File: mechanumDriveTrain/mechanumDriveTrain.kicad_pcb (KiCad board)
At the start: 4 copper layers, 88.9 x 99 mm, 38 parts, among them IC1 TCAN3414DR, J1 XT30U-M, J2 BM02B-SRSS-TB, J3 5 pin dupont, J4 5 pin dupont, U1 Teensy 4.1, U2 LD1117S50TR_SOT223

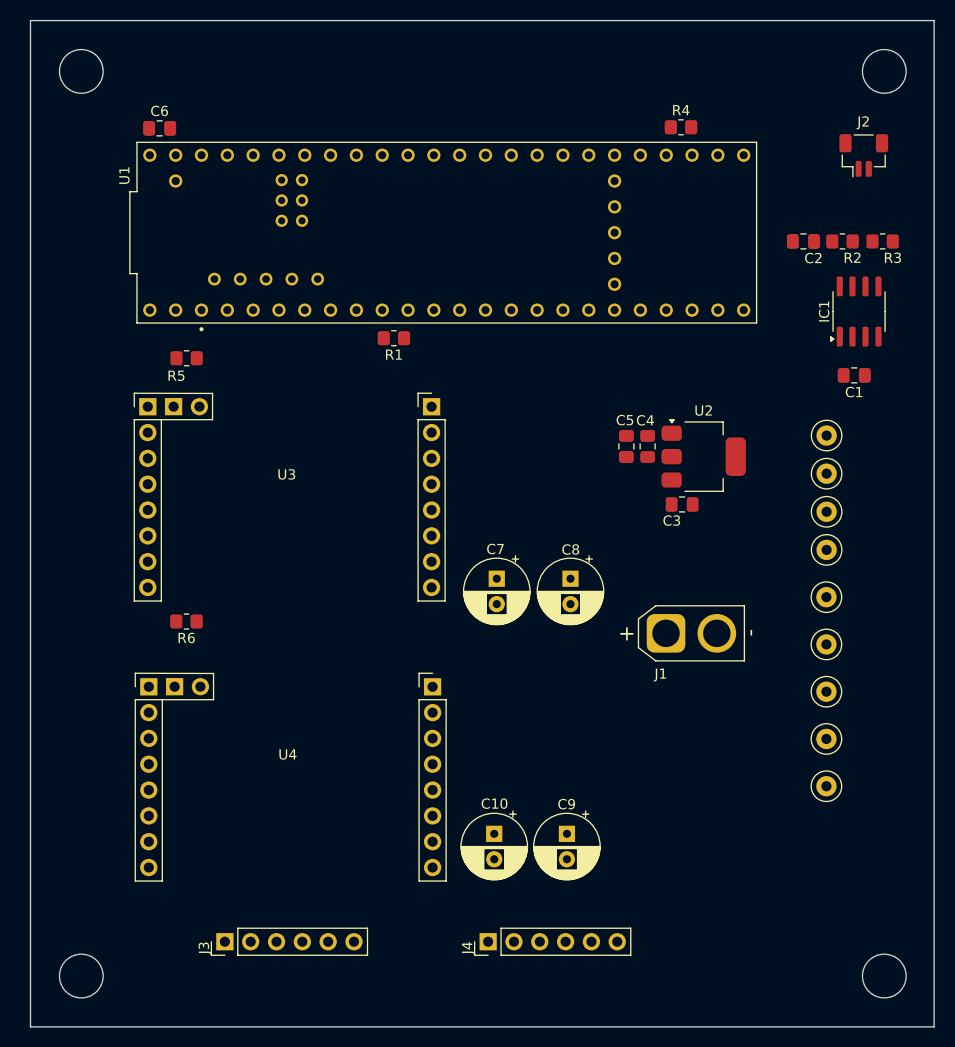
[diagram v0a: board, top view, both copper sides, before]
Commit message: Updated board size and layout
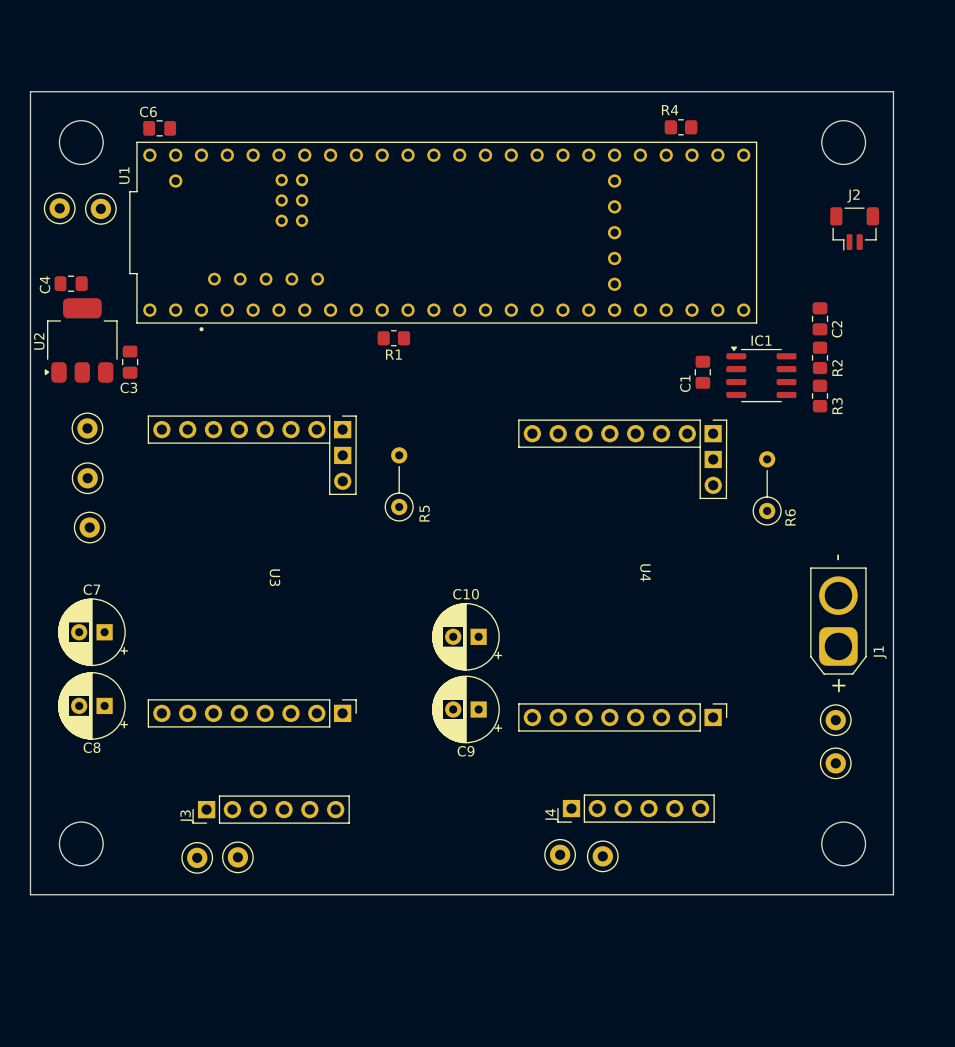
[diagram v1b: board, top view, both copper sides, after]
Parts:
- removed C5: 10 uF, Capacitor_SMD:C_0805_2012Metric_Pad1.18x1.45mm_HandSolder
- added TP10: ~, TestPoint:TestPoint_Loop_D1.80mm_Drill1.0mm_Beaded, F.Cu at (22.9, 38.5)
- added TP11: ~, TestPoint:TestPoint_Loop_D1.80mm_Drill1.0mm_Beaded, F.Cu at (25.8, 69.9)
- R5, R6: footprint Resistor_SMD:R_0805_2012Metric_Pad1.20x1.40mm_HandSolder -> Resistor_THT:R_Axial_DIN0207_L6.3mm_D2.5mm_P5.08mm_Vertical
- moved TP2 76.0 mm to (26.9, 38.5), turned to -90 degrees
- moved TP5 74.6 mm to (25.6, 60.1)
- moved TP3 72.8 mm to (25.6, 65.0)
- moved TP6 65.4 mm to (36.4, 102.4)
- moved U2 62.2 mm to (25.1, 51.5), turned to 90 degrees
- moved TP7 60.2 mm to (40.4, 102.3)
- moved C4 58.9 mm to (24.0, 45.9), turned to 180 degrees
- moved R6 58.2 mm to (92.5, 68.2), turned to 90 degrees
- moved C3 56.1 mm to (29.8, 53.6), turned to 90 degrees
- moved U4 48.9 mm to (94.0, 74.3), turned to -90 degrees
- moved C8 47.5 mm to (27.3, 87.4), turned to 180 degrees
- moved C7 38.9 mm to (27.3, 80.2), turned to 180 degrees
- moved TP8 28.6 mm to (72.1, 102.1)
- moved TP1 28.0 mm to (99.2, 88.8)
- moved U3 25.8 mm to (57.5, 73.9), turned to -90 degrees
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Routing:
- added copper zone on In1.Cu, net GND
- added copper zone on In2.Cu, net GND
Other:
- board size 88.9 x 99 mm -> 84.9 x 79 mm

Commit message: started routing
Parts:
- moved TP11 3.35 mm to (22.5, 69.5)
- moved TP3 3.15 mm to (22.5, 64.6)
- moved TP5 3.13 mm to (22.5, 59.7)
- moved C9 2.62 mm to (63.3, 85.3), turned to -90 degrees
- moved C8 2.15 mm to (27.3, 85.3), turned to -90 degrees
- moved C10 0.80 mm to (63.3, 80.6), turned to 90 degrees
- moved R5 0.70 mm to (55.6, 67.9)
- moved R6 0.60 mm to (91.9, 68.2)
- moved C7 0.45 mm to (27.3, 80.6), turned to 90 degrees
- moved R2 0.36 mm to (98.0, 53.0)
- moved R3 0.36 mm to (98.0, 56.7)
- moved C2 0.36 mm to (98.0, 49.1)
- moved TP10 0.30 mm to (23.2, 38.5)
- moved C1 0.22 mm to (86.3, 54.5)
- moved J2 0.20 mm to (101.3, 40.5)
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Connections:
- U1 pad 14: CS1 -> CS2
- U1 pad 15: CS2 -> CS1
- U4 pad 8: VCC -> unconnected-(U4-VM-Pad8)
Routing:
- net +3V3: track 0.00 -> 267.0 mm, vias 0 -> 2
- net EN_OUTB2: track 0.00 -> 71.1 mm
- net EN_OUTA2: track 0.00 -> 70.0 mm
- net FLT2: track 0.00 -> 34.7 mm
- net CS2: track 0.00 -> 34.5 mm
- net SLP2: track 0.00 -> 31.4 mm
- net +5V: track 0.00 -> 28.7 mm
- net CANN: track 0.00 -> 20.8 mm
- net CANP: track 0.00 -> 20.1 mm
- net VCC: track 0.00 -> 18.2 mm
- net C_RX: track 0.00 -> 14.1 mm
- net PWM2: track 0.00 -> 13.0 mm
- net DIR2: track 0.00 -> 13.0 mm
- net Net-(U3-VREF): track 0.00 -> 6.73 mm
- net Net-(U4-VREF): track 0.00 -> 6.54 mm
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- added copper zone on F.Cu, net +12V
- added copper zone on B.Cu, net GND
- added copper zone on F.Cu, net GND
- added copper zone on F.Cu, net OUTA2
- added copper zone on F.Cu, net OUTB2
- removed copper zone on In1.Cu, net GND
- removed copper zone on In2.Cu, net GND
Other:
- copper layers 4 -> 2

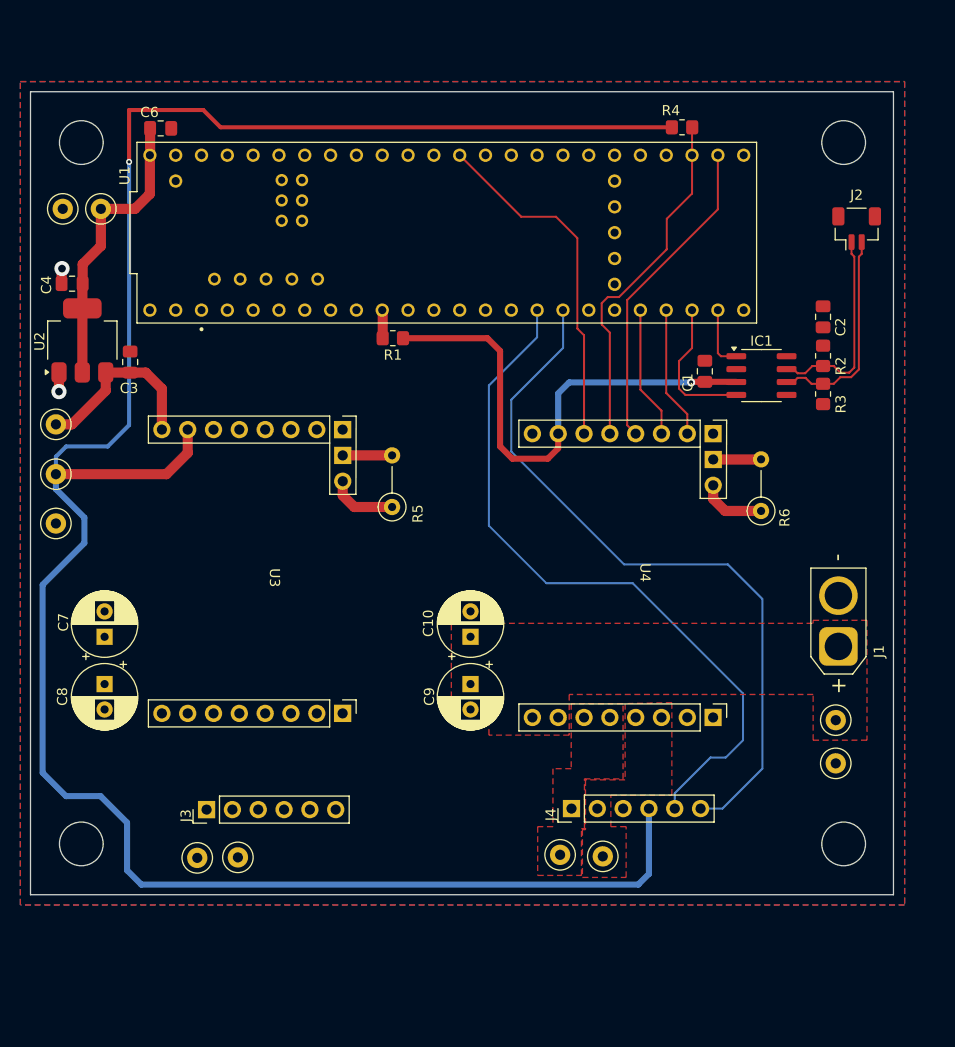
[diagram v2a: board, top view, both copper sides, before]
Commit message: revise Teensy footprint, first pass at routing
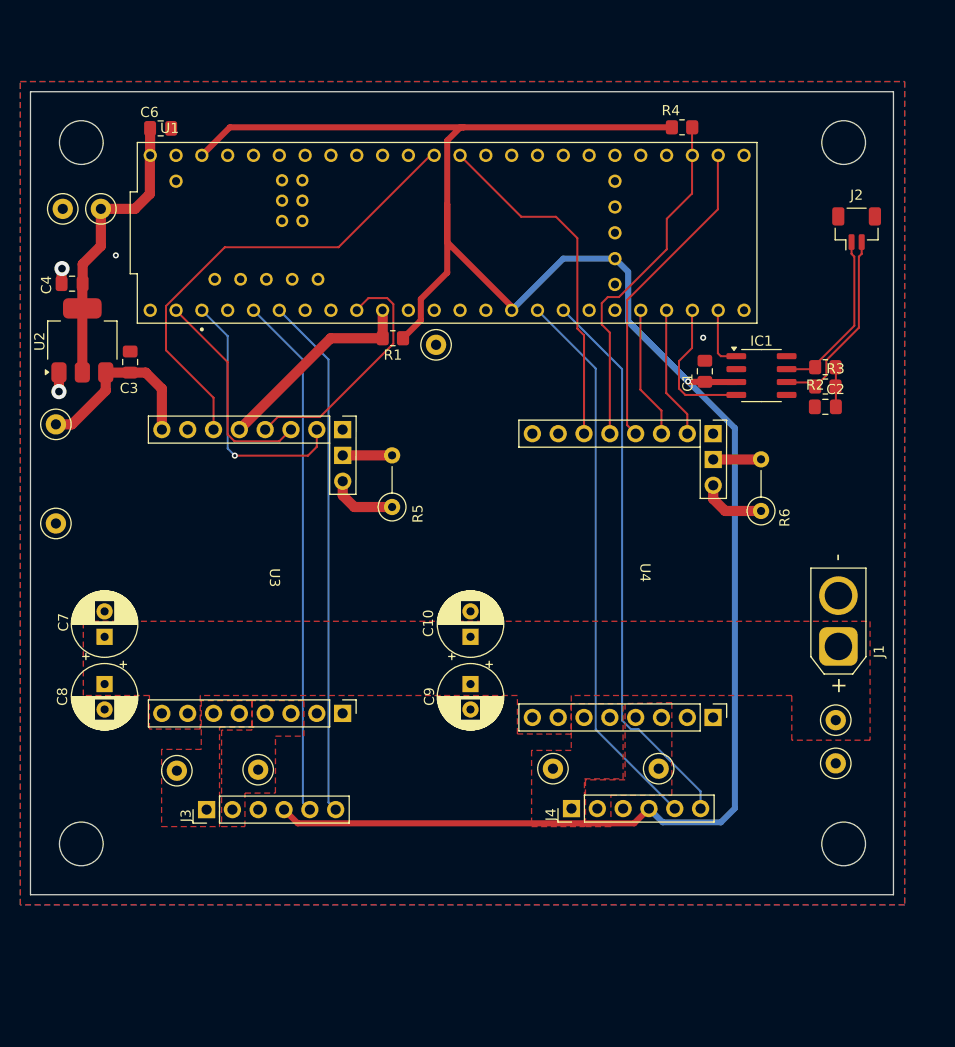
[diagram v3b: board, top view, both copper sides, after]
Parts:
- moved TP3 39.5 mm to (59.9, 51.9)
- moved TP9 10.2 mm to (81.8, 93.6)
- moved C2 8.86 mm to (98.2, 58.0), turned to 180 degrees
- moved TP7 8.85 mm to (42.4, 93.7)
- moved TP6 8.81 mm to (34.4, 93.8)
- moved TP8 8.50 mm to (71.4, 93.6)
- moved R2 1.14 mm to (98.2, 54.1), turned to 0 degrees
- moved R3 0.77 mm to (98.2, 56.0), turned to 180 degrees
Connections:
- U3 pad 7: +3V3 -> unconnected-(U3-3V3-Pad7)
- U4 pad 7: +3V3 -> unconnected-(U4-3V3-Pad7)
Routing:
- net +3V3: track 267.0 -> 214.8 mm, vias 2 -> 1
- net EN_OUTB1: track 0.00 -> 51.4 mm
- net EN_OUTA1: track 0.00 -> 51.4 mm
- net CS1: track 0.00 -> 46.3 mm
- net DIR1: track 0.00 -> 25.8 mm, vias 0 -> 1
- net SLP1: track 0.00 -> 24.4 mm
- net PWM1: track 0.00 -> 21.3 mm
- net FLT1: track 2.72 -> 20.5 mm
- net EN_OUTB2: track 71.1 -> 55.1 mm
- net EN_OUTA2: track 70.0 -> 54.6 mm
- net Net-(C2-Pad1): track 0.00 -> 3.86 mm
- net CANP: track 20.1 -> 16.4 mm
- net CANN: track 20.8 -> 18.5 mm
- net GND: vias 2 -> 4
- added copper zone on F.Cu, net OUTA1
- added copper zone on F.Cu, net OUTB1

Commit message: Updated routing, added labels
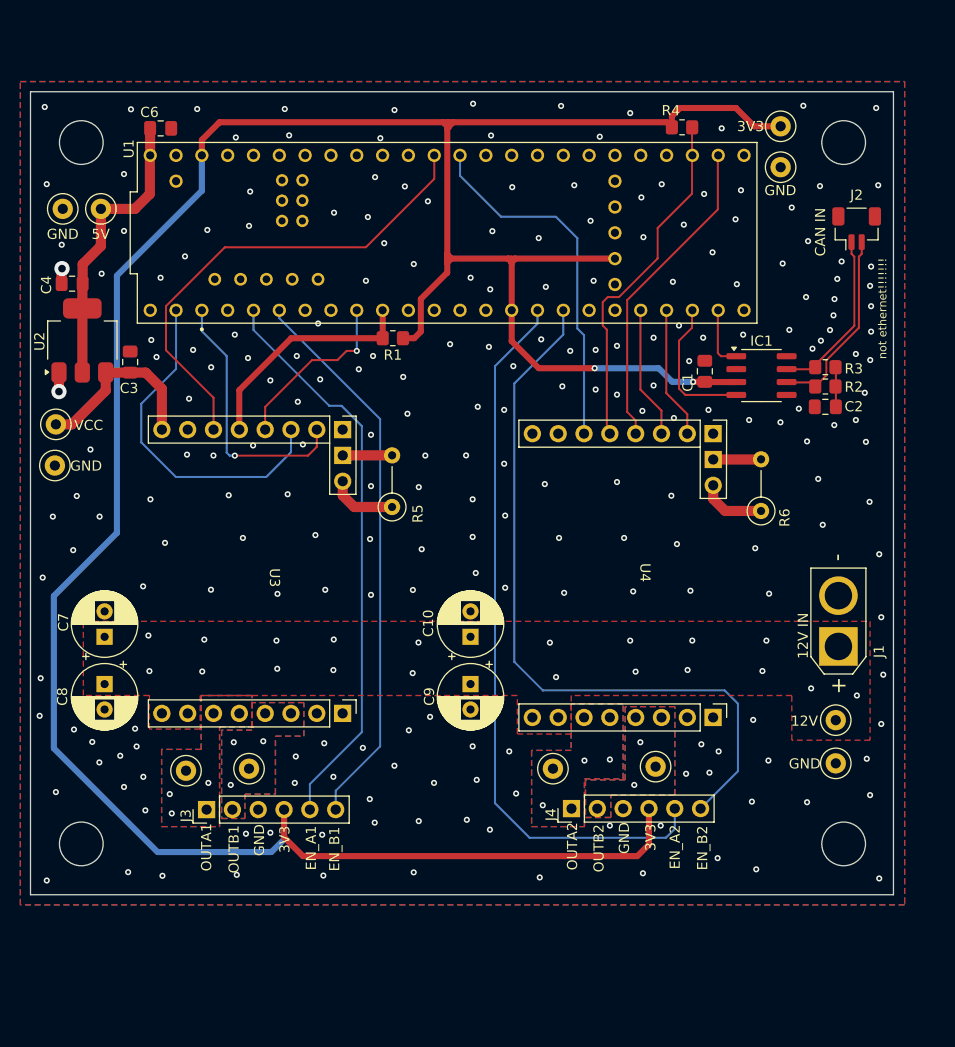
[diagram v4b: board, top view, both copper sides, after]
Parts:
- added G***: LOGO, LOGO, B.Cu at (75.8, 73.9)
- added TP12: ~, TestPoint:TestPoint_Loop_D1.80mm_Drill1.0mm_Beaded, F.Cu at (93.8, 34.4)
- moved TP3 40.1 mm to (93.8, 30.4)
- moved TP11 5.70 mm to (22.4, 63.8)
- moved TP7 0.91 mm to (41.5, 93.6)
- moved TP6 0.90 mm to (35.3, 93.8)
- moved TP9 0.36 mm to (81.5, 93.4)
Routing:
- net +3V3: track 214.8 -> 275.3 mm, vias 1 -> 2
- net EN_OUTB2: track 55.1 -> 72.1 mm
- net EN_OUTA2: track 54.6 -> 71.7 mm
- net PWM1: track 21.3 -> 33.8 mm
- net SLP1: track 24.4 -> 17.5 mm, vias 0 -> 1
- net EN_OUTA1: track 51.4 -> 56.4 mm
- net EN_OUTB1: track 51.4 -> 55.0 mm
- net FLT1: track 20.5 -> 22.8 mm
- net CS1: track 46.3 -> 48.0 mm
- net CS2: track 34.5 -> 35.6 mm
- net OUTB2: vias 0 -> 2
- net OUTB1: vias 0 -> 3
- net OUTA2: vias 0 -> 3
- net OUTA1: vias 0 -> 3
- net GND: vias 4 -> 229
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- added copper zone on B.Cu, net OUTA1
- added copper zone on B.Cu, net OUTA2
- added copper zone on B.Cu, net OUTB1
- added copper zone on B.Cu, net OUTB2
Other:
- board text added: "12V"
- board text added: "12V IN"
- board text added: "3V3"
- board text added: "5V"
- board text added: "CAN IN"
- board text added: "EN_A1"
- board text added: "EN_A2"
- board text added: "EN_B1"
- board text added: "EN_B2"
- board text added: "GND"
- board text added: "JC (yetanotheryay)"
- board text added: "Mechanum Drivebase"
- board text added: "OUTA1"
- board text added: "OUTA2"
- board text added: "OUTB1"
- board text added: "OUTB2"
- board text added: "SP (BigPierogi)"
- board text added: "V1"
- board text added: "VCC"
- board text added: "not ethernet!!!!!!!"

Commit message: Updated routing, created images, created gerbers
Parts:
- moved TP7 2.82 mm to (44.3, 93.3)
- moved R5 0.80 mm to (56.4, 67.9)
- moved C1 0.20 mm to (86.5, 54.5)
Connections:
- U1 pad 0: PWM1 -> unconnected-(U1-RX1-Pad0)
- U1 pad 11: unconnected-(U1-MOSI-Pad11) -> EN_OUTA1
- U1 pad 12: unconnected-(U1-MISO-Pad12) -> EN_OUTB1
- U1 pad 14: CS2 -> unconnected-(U1-A0-Pad14)
- U1 pad 15: CS1 -> unconnected-(U1-A1-Pad15)
- U1 pad 2: unconnected-(U1-OUT2-Pad2) -> PWM1
- U1 pad 23: unconnected-(U1-A9-Pad23) -> CS1
- U1 pad 3: EN_OUTA1 -> unconnected-(U1-LRCLK2-Pad3)
- U1 pad 4: EN_OUTB1 -> unconnected-(U1-BCLK2-Pad4)
- U1 pad 40: unconnected-(U1-A16-Pad40) -> CS2
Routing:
- net PWM1: track 33.8 -> 14.3 mm
- net CS1: track 48.0 -> 31.8 mm
- net CS2: track 35.6 -> 28.2 mm
- net EN_OUTA1: track 56.4 -> 55.2 mm
- net Net-(U3-VREFGND): track 4.85 -> 5.65 mm
- net Net-(U3-VREF): track 6.73 -> 7.53 mm
- net OUTB2: vias 2 -> 5
- net OUTB1: vias 3 -> 5
- net OUTA2: vias 3 -> 6
- net OUTA1: vias 3 -> 6
- net GND: vias 229 -> 241

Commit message: fixed pullup
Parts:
- R1, R4: value 60 -> 10K
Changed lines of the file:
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@@
 			)
 		)
-		(property "Value" "60"
+		(property "Value" "10K"
 			(at 0 1.65 0)
 			(layer "F.Fab")
@@
 			)
 		)
-		(property "Value" "60"
+		(property "Value" "10K"
 			(at 0 1.65 0)
 			(layer "F.Fab")
@@
 			(pts
 				(xy 41.7 91.8) (xy 38.8 91.8) (xy 38.8 98.5) (xy 41.1 98.5) (xy 41.1 96.1) (xy 46.896804 96.1) (xy 46.9 90.4)
-				(xy 46.9 90.4) (xy 46.9 87) (xy 41.8 87)
+				(xy 46.9 87) (xy 41.8 87)
 			)
 		)

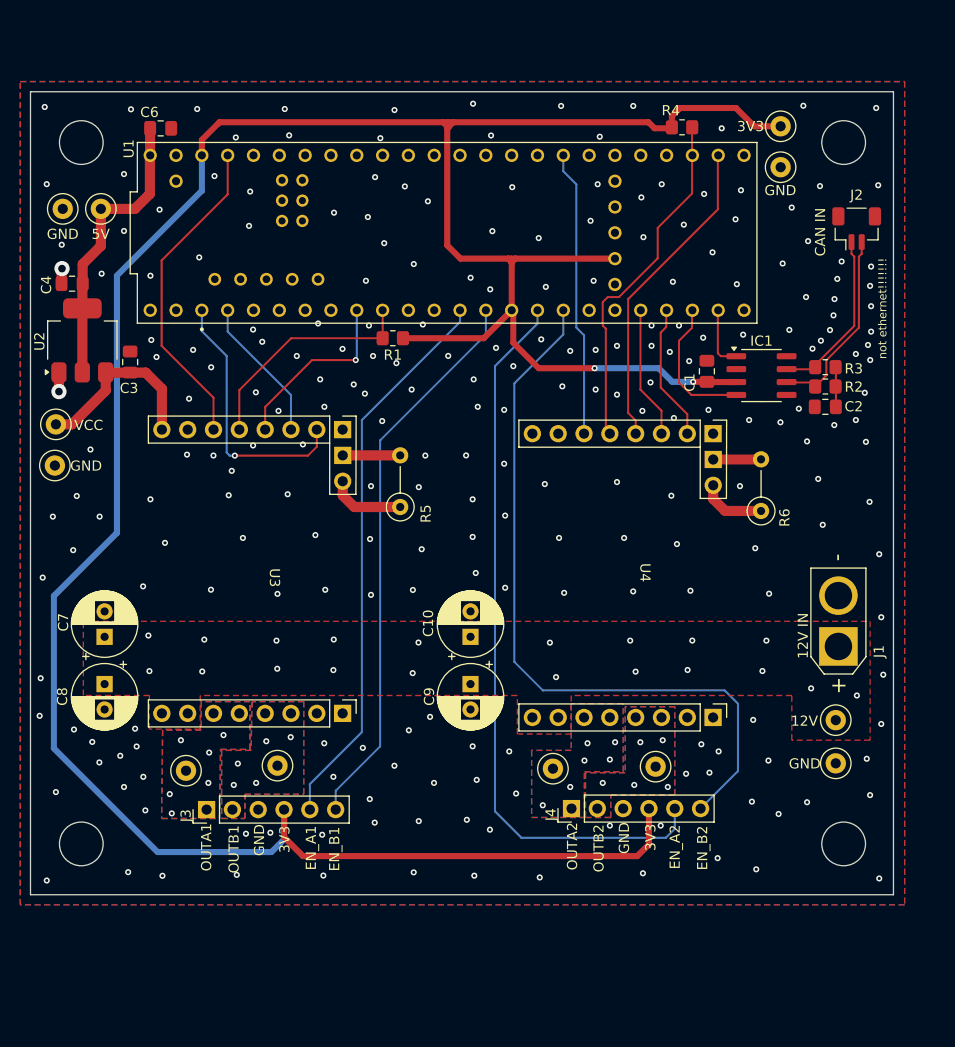
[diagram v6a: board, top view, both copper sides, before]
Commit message: neaten up stitching vias
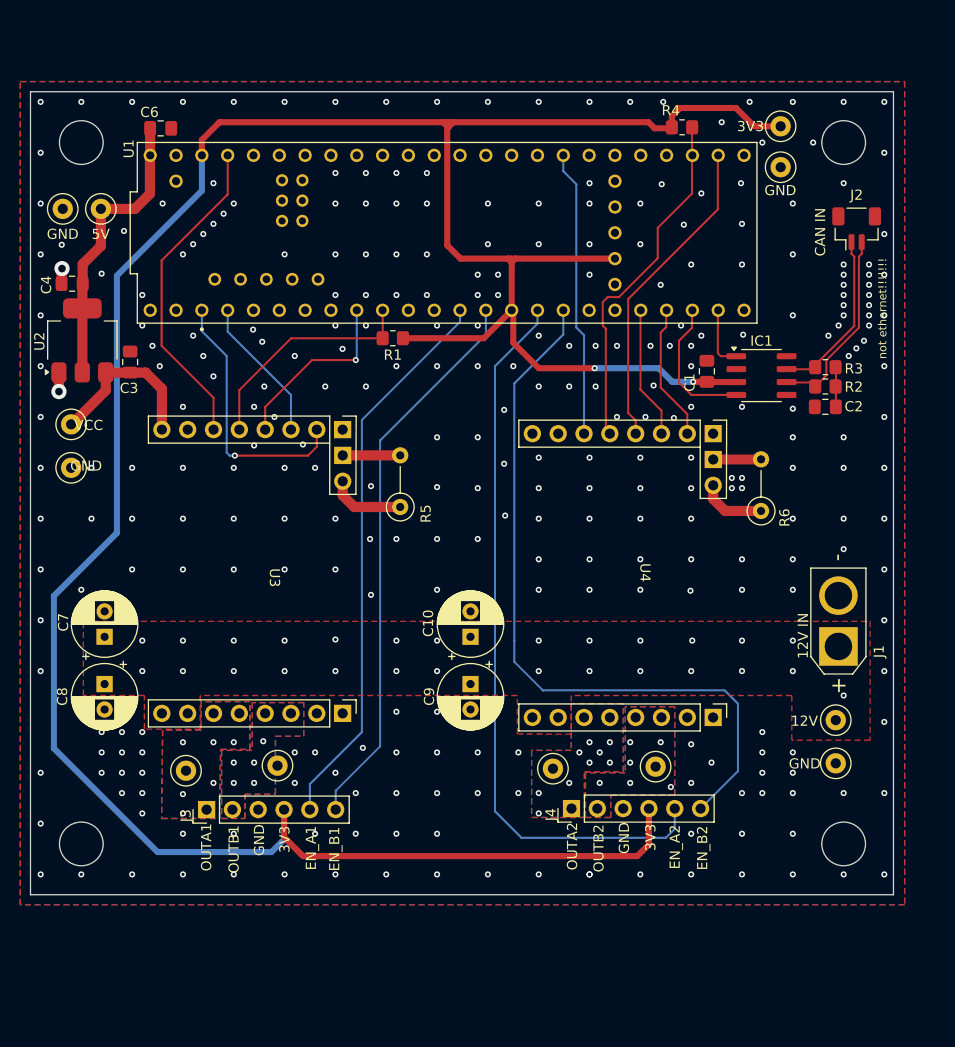
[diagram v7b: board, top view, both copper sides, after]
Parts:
- moved TP11 1.62 mm to (24.0, 64.0)
- moved TP5 1.50 mm to (24.0, 59.7)
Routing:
- net VCC: track 18.2 -> 16.7 mm
- net OUTB2: vias 5 -> 6
- net OUTA2: vias 6 -> 9
- net GND: vias 241 -> 304
- net +12V: vias 20 -> 27

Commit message: Updated gerbers, added step
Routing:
- net GND: vias 304 -> 303
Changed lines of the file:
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@@
 	)
 	(gr_text "VCC"
-		(at 24.3 60.4 0)
+		(at 25.8 60.4 0)
 		(layer "F.SilkS")
 		(effects
@@
 	)
 	(gr_text "GND"
-		(at 23.9 64.4 0)
+		(at 25.7 64.7 0)
 		(layer "F.SilkS")
 		(effects
@@
 		(size 0.6)
 		(drill 0.3)
-		(layers "F.Cu" "B.Cu")
-		(free yes)
-		(net 1)
-	)
-	(via
-		(at 26 64)
-		(size 0.6)
-		(drill 0.3)
